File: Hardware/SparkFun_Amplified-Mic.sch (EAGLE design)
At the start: 15 parts, among them M1 MIC9.7MM, U1 OPA344

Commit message: Ready for Review
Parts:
- M1: device SparkFun:MIC9.7MM -> SparkFun-Sensors:MIC9.7MM
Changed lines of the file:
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@@
 <grid distance="0.1" unitdist="inch" unit="inch" style="lines" multiple="1" display="no" altdistance="0.01" altunitdist="inch" altunit="inch"/>
 <layers>
-<layer number="1" name="Top" color="4" fill="1" visible="yes" active="no"/>
-<layer number="2" name="Route2" color="1" fill="3" visible="yes" active="no"/>
-<layer number="3" name="Route3" color="4" fill="3" visible="yes" active="no"/>
-<layer number="4" name="Route4" color="1" fill="4" visible="yes" active="no"/>
-<layer number="5" name="Route5" color="4" fill="4" visible="yes" active="no"/>
-<layer number="6" name="Route6" color="1" fill="8" visible="yes" active="no"/>
-<layer number="7" name="Route7" color="4" fill="8" visible="yes" active="no"/>
-<layer number="8" name="Route8" color="1" fill="2" visible="yes" active="no"/>
-<layer number="9" name="Route9" color="4" fill="2" visible="yes" active="no"/>
-<layer number="10" name="Route10" color="1" fill="7" visible="yes" active="no"/>
-<layer number="11" name="Route11" color="4" fill="7" visible="yes" active="no"/>
-<layer number="12" name="Route12" color="1" fill="5" visible="yes" active="no"/>
-<layer number="13" name="Route13" color="4" fill="5" visible="yes" active="no"/>
-<layer number="14" name="Route14" color="1" fill="6" visible="yes" active="no"/>
-<layer number="15" name="Route15" color="4" fill="6" visible="yes" active="no"/>
-<layer number="16" name="Bottom" color="1" fill="1" visible="yes" active="no"/>
-<layer number="17" name="Pads" color="2" fill="1" visible="yes" active="no"/>
-<layer number="18" name="Vias" color="2" fill="1" visible="yes" active="no"/>
-<layer number="19" name="Unrouted" color="6" fill="1" visible="yes" active="no"/>
-<layer number="20" name="Dimension" color="15" fill="1" visible="yes" active="no"/>
-<layer number="21" name="tPlace" color="16" fill="1" visible="yes" active="no"/>
-<layer number="22" name="bPlace" color="14" fill="1" visible="yes" active="no"/>
-<layer number="23" name="tOrigins" color="15" fill="1" visible="yes" active="no"/>
-<layer number="24" name="bOrigins" color="15" fill="1" visible="yes" active="no"/>
-<layer number="25" name="tNames" color="7" fill="1" visible="yes" active="no"/>
-<layer number="26" name="bNames" color="7" fill="1" visible="yes" active="no"/>
-<layer number="27" name="tValues" color="7" fill="1" visible="yes" active="no"/>
-<layer number="28" name="bValues" color="7" fill="1" visible="yes" active="no"/>
+<layer number="1" name="Top" color="4" fill="1" visible="no" active="no"/>
+<layer number="2" name="Route2" color="1" fill="3" visible="no" active="no"/>
+<layer number="3" name="Route3" color="4" fill="3" visible="no" active="no"/>
+<layer number="4" name="Route4" color="1" fill="4" visible="no" active="no"/>
+<layer number="5" name="Route5" color="4" fill="4" visible="no" active="no"/>
+<layer number="6" name="Route6" color="1" fill="8" visible="no" active="no"/>
+<layer number="7" name="Route7" color="4" fill="8" visible="no" active="no"/>
+<layer number="8" name="Route8" color="1" fill="2" visible="no" active="no"/>
+<layer number="9" name="Route9" color="4" fill="2" visible="no" active="no"/>
+<layer number="10" name="Route10" color="1" fill="7" visible="no" active="no"/>
+<layer number="11" name="Route11" color="4" fill="7" visible="no" active="no"/>
+<layer number="12" name="Route12" color="1" fill="5" visible="no" active="no"/>
+<layer number="13" name="Route13" color="4" fill="5" visible="no" active="no"/>
+<layer number="14" name="Route14" color="1" fill="6" visible="no" active="no"/>
+<layer number="15" name="Route15" color="4" fill="6" visible="no" active="no"/>
+<layer number="16" name="Bottom" color="1" fill="1" visible="no" active="no"/>
+<layer number="17" name="Pads" color="2" fill="1" visible="no" active="no"/>
+<layer number="18" name="Vias" color="2" fill="1" visible="no" active="no"/>
+<layer number="19" name="Unrouted" color="6" fill="1" visible="no" active="no"/>
+<layer number="20" name="Dimension" color="15" fill="1" visible="no" active="no"/>
+<layer number="21" name="tPlace" color="16" fill="1" visible="no" active="no"/>
+<layer number="22" name="bPlace" color="14" fill="1" visible="no" active="no"/>
+<layer number="23" name="tOrigins" color="15" fill="1" visible="no" active="no"/>
+<layer number="24" name="bOrigins" color="15" fill="1" visible="no" active="no"/>
+<layer number="25" name="tNames" color="7" fill="1" visible="no" active="no"/>
+<layer number="26" name="bNames" color="7" fill="1" visible="no" active="no"/>
+<layer number="27" name="tValues" color="7" fill="1" visible="no" active="no"/>
+<layer number="28" name="bValues" color="7" fill="1" visible="no" active="no"/>
 <layer number="29" name="tStop" color="7" fill="3" visible="no" active="no"/>
 <layer number="30" name="bStop" color="7" fill="6" visible="no" active="no"/>
@@
 <layer number="35" name="tGlue" color="7" fill="4" visible="no" active="no"/>
 <layer number="36" name="bGlue" color="7" fill="5" visible="no" active="no"/>
-<layer number="37" name="tTest" color="7" fill="1" visible="yes" active="no"/>
-<layer number="38" name="bTest" color="7" fill="1" visible="yes" active="no"/>
+<layer number="37" name="tTest" color="7" fill="1" visible="no" active="no"/>
+<layer number="38" name="bTest" color="7" fill="1" visible="no" active="no"/>
 <layer number="39" name="tKeepout" color="4" fill="11" visible="no" active="no"/>
 <layer number="40" name="bKeepout" color="1" fill="11" visible="no" active="no"/>
@@
 <layer number="44" name="Drills" color="7" fill="1" visible="no" active="no"/>
 <layer number="45" name="Holes" color="7" fill="1" visible="no" active="no"/>
-<layer number="46" name="Milling" color="3" fill="1" visible="yes" active="no"/>
-<layer number="47" name="Measures" color="7" fill="1" visible="yes" active="no"/>
-<layer number="48" name="Document" color="7" fill="1" visible="yes" active="no"/>
-<layer number="49" name="Reference" color="7" fill="1" visible="yes" active="no"/>
-<layer number="50" name="dxf" color="7" fill="1" visible="yes" active="no"/>
-<layer number="51" name="tDocu" color="6" fill="1" visible="yes" active="no"/>
-<layer number="52" name="bDocu" color="7" fill="1" visible="yes" active="no"/>
-<layer number="53" name="tGND_GNDA" color="7" fill="9" visible="yes" active="no"/>
-<layer number="54" name="bGND_GNDA" color="1" fill="9" visible="yes" active="no"/>
-<layer number="56" name="wert" color="7" fill="1" visible="yes" active="no"/>
-<layer number="57" name="tCAD" color="7" fill="1" visible="yes" active="no"/>
-<layer number="59" name="tCarbon" color="7" fill="1" visible="yes" active="no"/>
-<layer number="60" name="bCarbon" color="7" fill="1" visible="yes" active="no"/>
+<layer number="46" name="Milling" color="3" fill="1" visible="no" active="no"/>
+<layer number="47" name="Measures" color="7" fill="1" visible="no" active="no"/>
+<layer number="48" name="Document" color="7" fill="1" visible="no" active="no"/>
+<layer number="49" name="Reference" color="7" fill="1" visible="no" active="no"/>
+<layer number="50" name="dxf" color="7" fill="1" visible="no" active="no"/>
+<layer number="51" name="tDocu" color="6" fill="1" visible="no" active="no"/>
+<layer number="52" name="bDocu" color="7" fill="1" visible="no" active="no"/>
+<layer number="53" name="tGND_GNDA" color="7" fill="9" visible="no" active="no"/>
+<layer number="54" name="bGND_GNDA" color="1" fill="9" visible="no" active="no"/>
+<layer number="56" name="wert" color="7" fill="1" visible="no" active="no"/>
+<layer number="57" name="tCAD" color="7" fill="1" visible="no" active="no"/>
+<layer number="59" name="tCarbon" color="7" fill="1" visible="no" active="no"/>
+<layer number="60" name="bCarbon" color="7" fill="1" visible="no" active="no"/>
 <layer number="90" name="Modules" color="5" fill="1" visible="yes" active="yes"/>
 <layer number="91" name="Nets" color="2" fill="1" visible="yes" active="yes"/>
@@
 <layer number="113" name="IDFDebug" color="4" fill="1" visible="yes" active="yes"/>
 <layer number="116" name="Patch_BOT" color="9" fill="4" visible="yes" active="yes"/>
+<layer number="118" name="Rect_Pads" color="7" fill="1" visible="yes" active="yes"/>
 <layer number="121" name="_tsilk" color="7" fill="1" visible="yes" active="yes"/>
 <layer number="122" name="_bsilk" color="7" fill="1" visible="yes" active="yes"/>
@@
 <parts>
 <part name="FRAME1" library="SparkFun-Aesthetics" deviceset="FRAME-LETTER" device=""/>
-<part name="M1" library="SparkFun" deviceset="MIC" device="9.7MM"/>
+<part name="M1" library="SparkFun-Sensors" deviceset="MIC" device="9.7MM"/>
 <part name="U1" library="SparkFun" deviceset="OPA344" device=""/>
 <part name="C1" library="SparkFun-Capacitors" deviceset="4.7UF-6.3V-10%(0603)" device="0603" value="4.7uF"/>

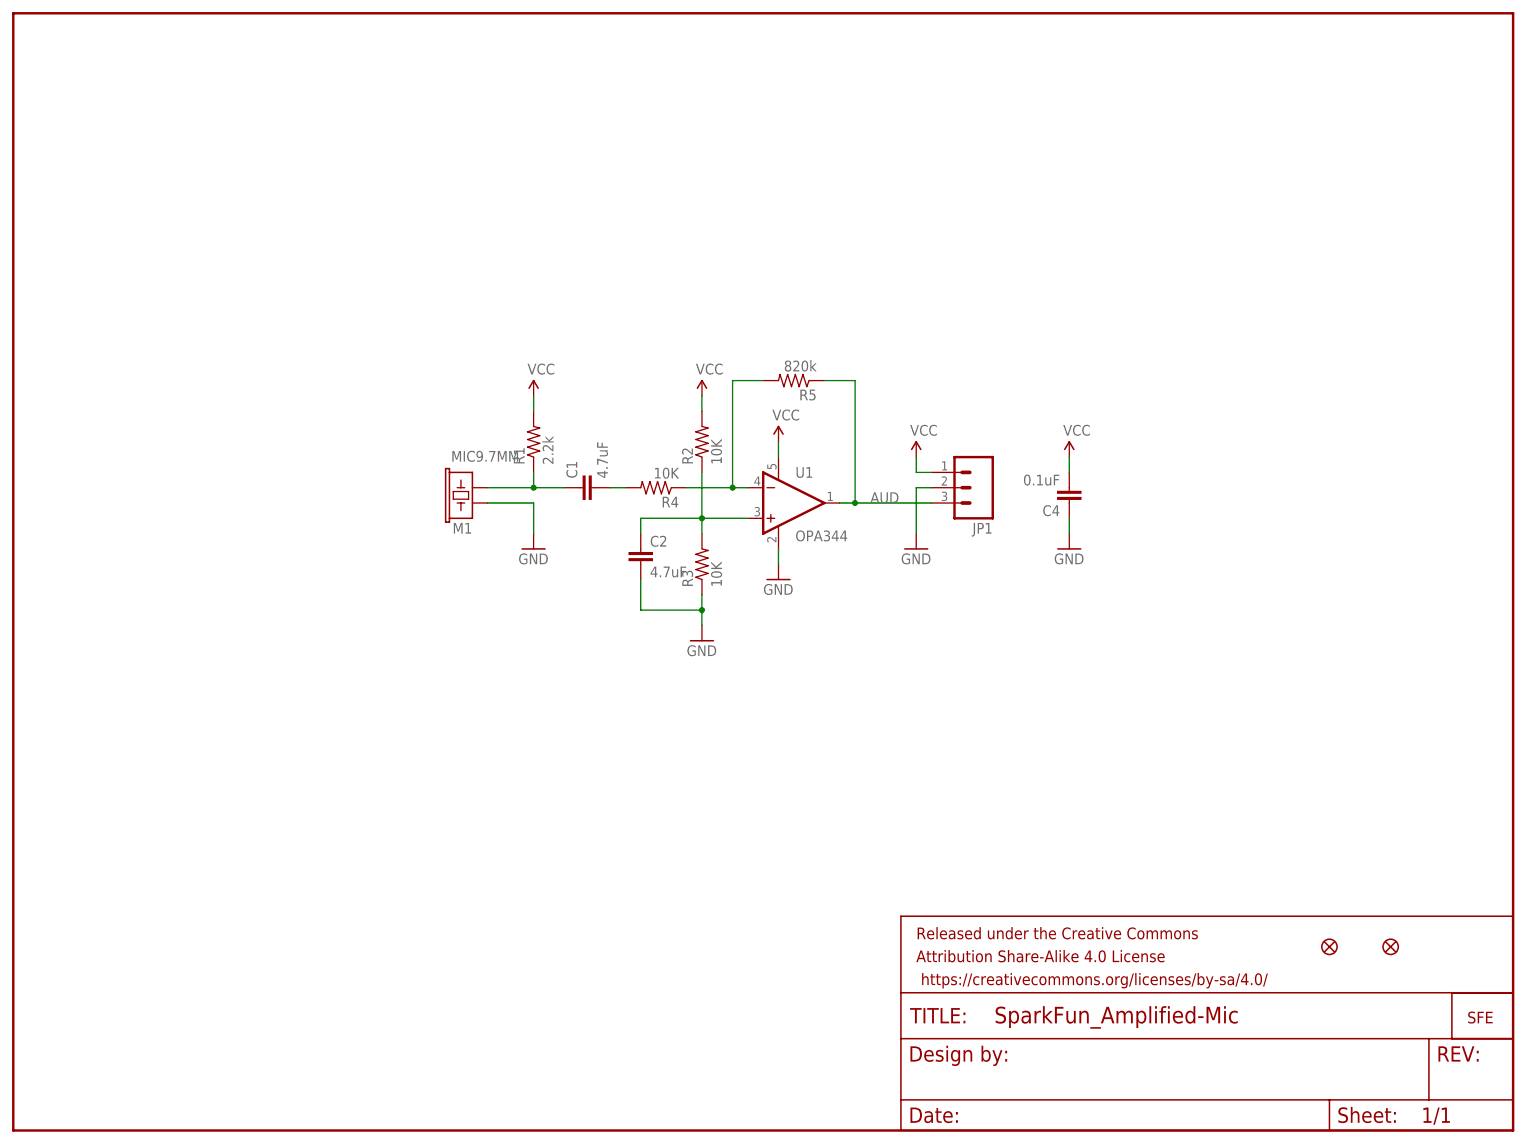
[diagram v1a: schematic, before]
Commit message: Revised Board and Schematic per Design review 2/8/2016
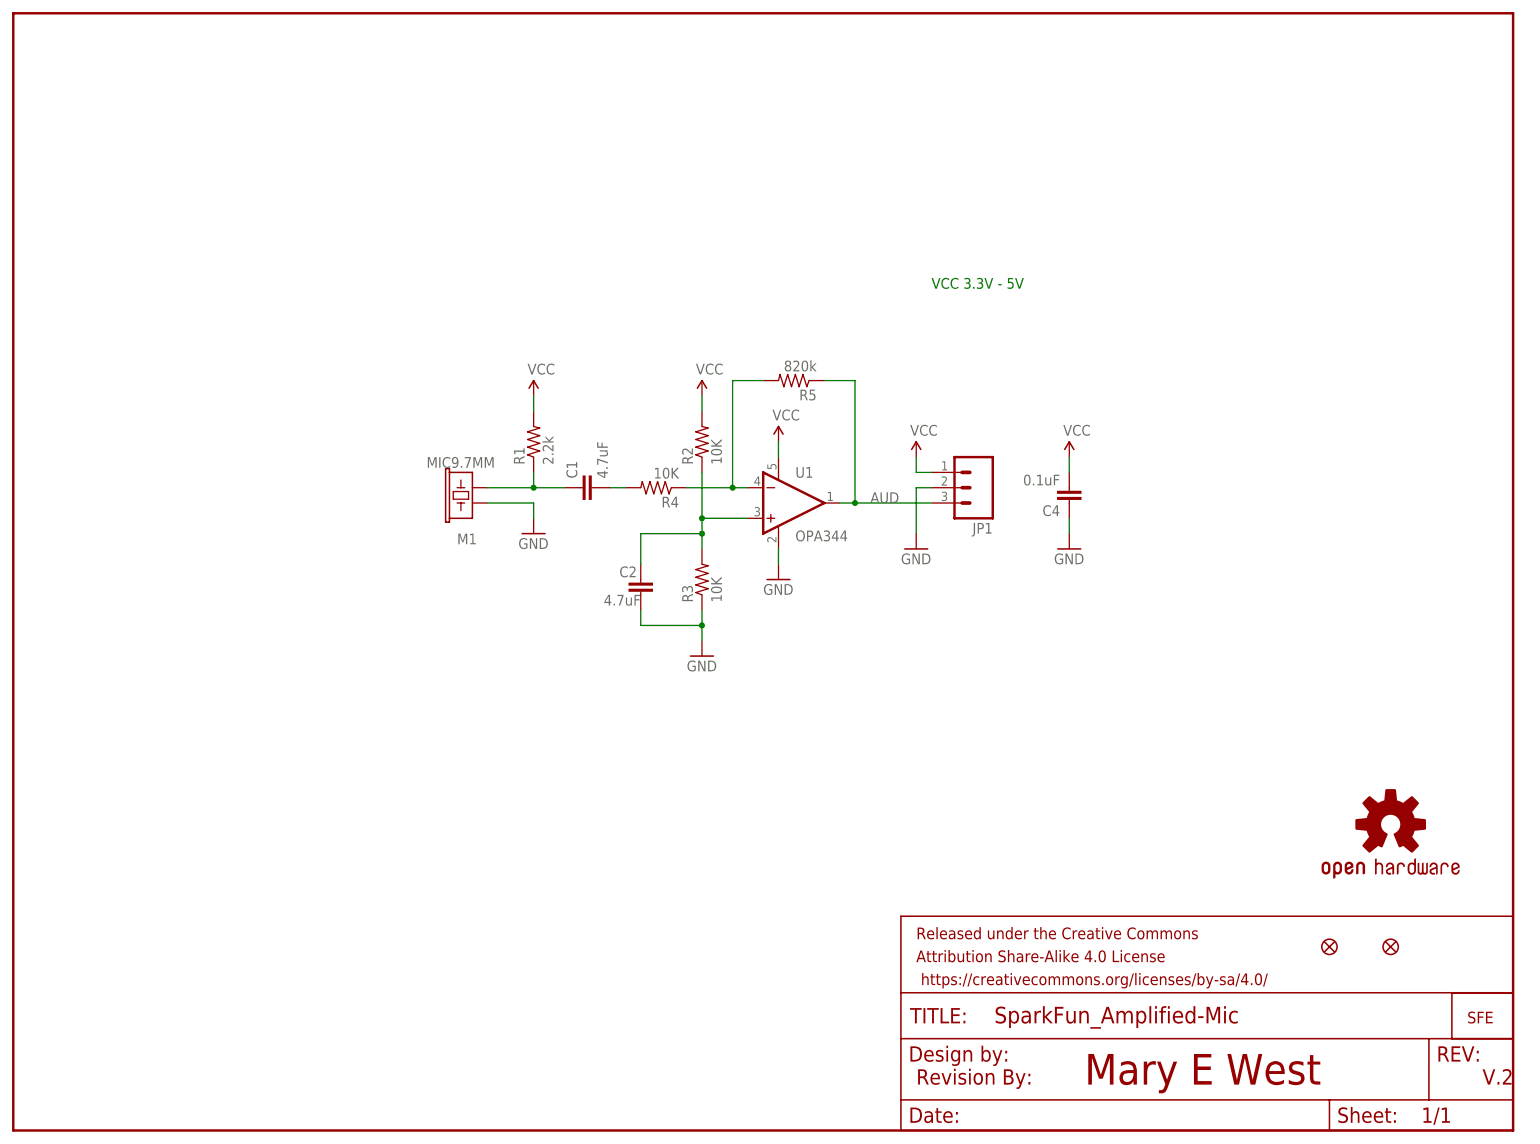
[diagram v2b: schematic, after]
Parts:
- added LOGO1: OSHW-LOGOMINI, SparkFun-Aesthetics:OSHW-LOGOMINI
- added U$2: REVISION, SparkFun-Aesthetics:REVISION
- C4: device SparkFun:CAP0402-CAP -> SparkFun-Capacitors:0.1UF-25V(+80/-20%)(0603)
- U1: device SparkFun:OPA344 -> SparkFun-AnalogIC:OPA344
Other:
- note added: "Mary E West"
- note added: "V.2"
- note added: "VCC 3.3V - 5V"
- moved on the sheet: C2, R3
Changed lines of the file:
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@@
 <setting verticaltext="up"/>
 </settings>
-<grid distance="0.1" unitdist="inch" unit="inch" style="lines" multiple="1" display="no" altdistance="0.01" altunitdist="inch" altunit="inch"/>
+<grid distance="0.1" unitdist="inch" unit="inch" style="lines" multiple="1" display="yes" altdistance="0.01" altunitdist="inch" altunit="inch"/>
 <layers>
 <layer number="1" name="Top" color="4" fill="1" visible="no" active="no"/>
@@
 <part name="FRAME1" library="SparkFun-Aesthetics" deviceset="FRAME-LETTER" device=""/>
 <part name="M1" library="SparkFun-Sensors" deviceset="MIC" device="9.7MM"/>
-<part name="U1" library="SparkFun" deviceset="OPA344" device=""/>
+<part name="U1" library="SparkFun-AnalogIC" deviceset="OPA344" device=""/>
 <part name="C1" library="SparkFun-Capacitors" deviceset="4.7UF-6.3V-10%(0603)" device="0603" value="4.7uF"/>
 <part name="R1" library="SparkFun-Resistors" deviceset="2.2KOHM-1/10W-1%(0603)" device="" value="2.2k"/>
@@
 <part name="R5" library="SparkFun-Resistors" deviceset="2.2MOHM-1/10W-5%(0603)" device="" value="820k"/>
 <part name="C2" library="SparkFun-Capacitors" deviceset="4.7UF-6.3V-10%(0603)" device="0603" value="4.7uF"/>
-<part name="C4" library="SparkFun" deviceset="CAP" device="0402-CAP" value="0.1uF"/>
+<part name="C4" library="SparkFun-Capacitors" deviceset="0.1UF-25V(+80/-20%)(0603)" device="" value="0.1uF"/>
 <part name="GND3" library="SparkFun" deviceset="GND" device=""/>
 <part name="GND4" library="SparkFun" deviceset="GND" device=""/>
@@
 <part name="JP2" library="SparkFun-Aesthetics" deviceset="FIDUCIAL" device="UFIDUCIAL"/>
 <part name="JP3" library="SparkFun-Aesthetics" deviceset="FIDUCIAL" device="UFIDUCIAL"/>
+<part name="LOGO1" library="SparkFun-Aesthetics" deviceset="OSHW-LOGO" device="MINI"/>
+<part name="U$2" library="SparkFun-Aesthetics" deviceset="REVISION" device=""/>
 </parts>
 <sheets>
 <sheet>
 <plain>
+<text x="152.4" y="139.7" size="1.778" layer="91">VCC 3.3V - 5V</text>
+<text x="243.84" y="7.62" size="2.54" layer="94">V.2</text>
+<text x="177.8" y="7.62" size="5.08" layer="94">Mary E West</text>
 </plain>
 <instances>
@@
 <instance part="FRAME1" gate="V" x="147.32" y="0"/>
 <instance part="M1" gate="G$1" x="76.2" y="106.68" smashed="yes" rot="MR270">
-<attribute name="NAME" x="72.898" y="100.838" size="1.778" layer="95" rot="MR180"/>
-<attribute name="VALUE" x="72.644" y="112.776" size="1.778" layer="96" rot="MR180"/>
+<attribute name="NAME" x="73.66" y="99.06" size="1.778" layer="95" rot="MR180"/>
+<attribute name="VALUE" x="68.58" y="111.76" size="1.778" layer="96" rot="MR180"/>
 </instance>
 <instance part="U1" gate="G$1" x="127" y="104.14" smashed="yes">
@@
 <instance part="U$1" gate="G$1" x="241.3" y="17.78"/>
 <instance part="R2" gate="G$1" x="114.3" y="114.3" rot="R90"/>
-<instance part="R3" gate="G$1" x="114.3" y="93.98" rot="R90"/>
+<instance part="R3" gate="G$1" x="114.3" y="91.44" rot="R90"/>
 <instance part="R4" gate="G$1" x="106.68" y="106.68" rot="R180"/>
 <instance part="R5" gate="G$1" x="129.54" y="124.46" rot="R180"/>
-<instance part="C2" gate="G$1" x="104.14" y="93.98"/>
+<instance part="C2" gate="G$1" x="104.14" y="88.9" smashed="yes">
+<attribute name="NAME" x="100.584" y="91.821" size="1.778" layer="95"/>
+<attribute name="VALUE" x="104.14" y="88.9" size="1.778" layer="96" rot="R180"/>
+</instance>
 <instance part="C4" gate="G$1" x="175.26" y="106.68" rot="R180"/>
 <instance part="GND3" gate="1" x="175.26" y="96.52"/>
-<instance part="GND4" gate="1" x="114.3" y="81.28"/>
+<instance part="GND4" gate="1" x="114.3" y="78.74"/>
 <instance part="P+4" gate="1" x="114.3" y="121.92"/>
 <instance part="P+5" gate="1" x="175.26" y="111.76"/>
-<instance part="GND5" gate="1" x="86.36" y="96.52"/>
+<instance part="GND5" gate="1" x="86.36" y="99.06"/>
 <instance part="JP2" gate="G$1" x="228.6" y="30.48"/>
 <instance part="JP3" gate="G$1" x="218.44" y="30.48"/>
+<instance part="LOGO1" gate="G$1" x="228.6" y="50.8"/>
+<instance part="U$2" gate="G$1" x="149.86" y="7.62"/>
 </instances>
 <busses>
@@
 </segment>
 <segment>
-<wire x1="104.14" y1="91.44" x2="104.14" y2="86.36" width="0.1524" layer="91"/>
-<wire x1="104.14" y1="86.36" x2="114.3" y2="86.36" width="0.1524" layer="91"/>
-<wire x1="114.3" y1="86.36" x2="114.3" y2="88.9" width="0.1524" layer="91"/>
+<wire x1="104.14" y1="86.36" x2="104.14" y2="83.82" width="0.1524" layer="91"/>
+<wire x1="104.14" y1="83.82" x2="114.3" y2="83.82" width="0.1524" layer="91"/>
 <wire x1="114.3" y1="83.82" x2="114.3" y2="86.36" width="0.1524" layer="91"/>
-<junction x="114.3" y="86.36"/>
+<wire x1="114.3" y1="81.28" x2="114.3" y2="83.82" width="0.1524" layer="91"/>
+<junction x="114.3" y="83.82"/>
 <pinref part="C2" gate="G$1" pin="2"/>
 <pinref part="R3" gate="G$1" pin="1"/>
@@
 </segment>
 <segment>
-<wire x1="86.36" y1="104.14" x2="86.36" y2="99.06" width="0.1524" layer="91"/>
+<wire x1="86.36" y1="104.14" x2="86.36" y2="101.6" width="0.1524" layer="91"/>
 <wire x1="86.36" y1="104.14" x2="78.74" y2="104.14" width="0.1524" layer="91"/>
 <pinref part="GND5" gate="1" pin="GND"/>
@@
 <wire x1="114.3" y1="109.22" x2="114.3" y2="101.6" width="0.1524" layer="91"/>
 <wire x1="114.3" y1="101.6" x2="114.3" y2="99.06" width="0.1524" layer="91"/>
-<wire x1="104.14" y1="99.06" x2="104.14" y2="101.6" width="0.1524" layer="91"/>
-<wire x1="104.14" y1="101.6" x2="114.3" y2="101.6" width="0.1524" layer="91"/>
+<wire x1="114.3" y1="99.06" x2="114.3" y2="96.52" width="0.1524" layer="91"/>
 <wire x1="121.92" y1="101.6" x2="114.3" y2="101.6" width="0.1524" layer="91"/>
 <junction x="114.3" y="101.6"/>
 <pinref part="R2" gate="G$1" pin="1"/>
 <pinref part="R3" gate="G$1" pin="2"/>
+<pinref part="U1" gate="G$1" pin="+IN"/>
 <pinref part="C2" gate="G$1" pin="1"/>
-<pinref part="U1" gate="G$1" pin="+IN"/>
-</segment>
-</net>
+<wire x1="104.14" y1="93.98" x2="104.14" y2="99.06" width="0.1524" layer="91"/>
+<wire x1="104.14" y1="99.06" x2="114.3" y2="99.06" width="0.1524" layer="91"/>
+<junction x="114.3" y="99.06"/>
+</segment>
+</net>
